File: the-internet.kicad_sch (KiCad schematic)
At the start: 9 parts, among them J1 POWER, J2 LOLIN-C3-MINI (L), J3 LOLIN-C3-MINI (R), Q1 KSC1815YTA

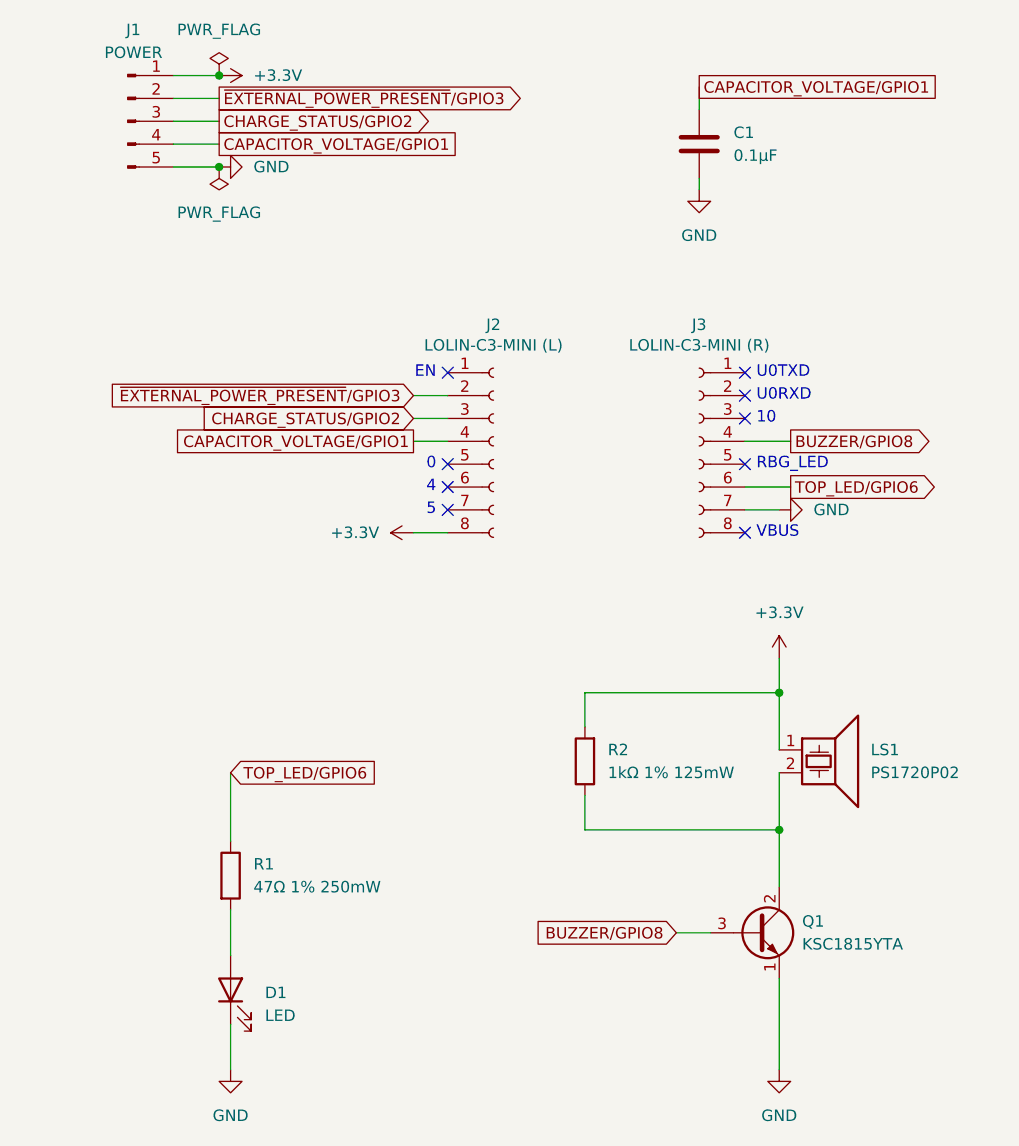
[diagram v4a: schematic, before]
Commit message: Add resistor to buzzer transistor
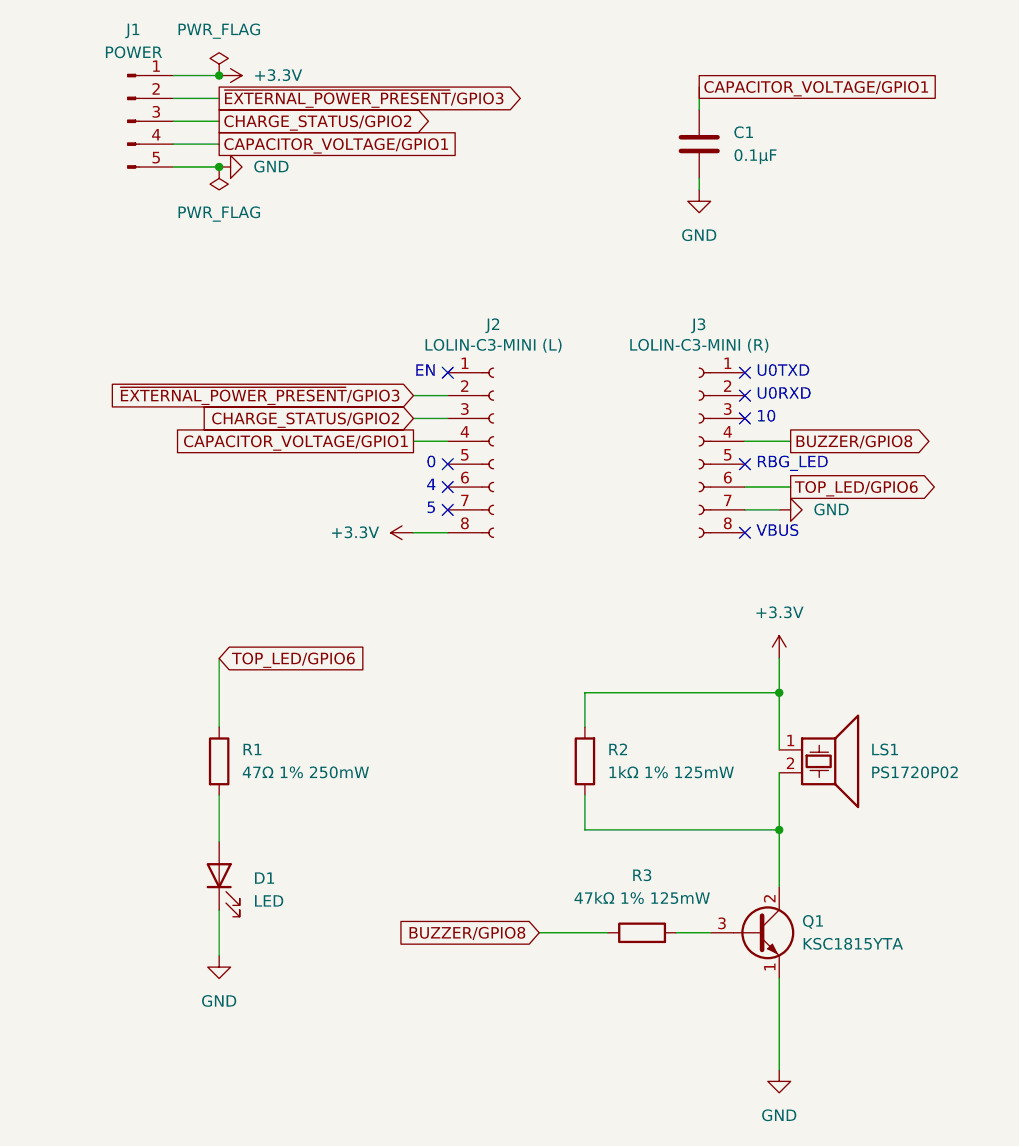
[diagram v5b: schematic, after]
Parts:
- added R3: 47kΩ 1% 125mW, Resistor_SMD:R_0805_2012Metric_Pad1.20x1.40mm_HandSolder, symbol Device:R
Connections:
- net BUZZER/GPIO8: now also R3.1; no longer Q1.3 (B)
- new net: Q1.3 (B), R3.2
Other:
- moved on the sheet: D1, R1
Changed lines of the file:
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@@
 	(wire
 		(pts
-			(xy 20.32 91.44) (xy 20.32 99.06)
+			(xy 19.05 78.74) (xy 19.05 86.36)
+		)
+		(stroke
+			(width 0)
+			(type default)
+		)
+	)
+	(wire
+		(pts
+			(xy 54.61 109.22) (xy 62.23 109.22)
 		)
 		(stroke
@@
 	(wire
 		(pts
-			(xy 20.32 106.68) (xy 20.32 111.76)
+			(xy 19.05 93.98) (xy 19.05 99.06)
 		)
 		(stroke
@@
 	(wire
 		(pts
-			(xy 20.32 119.38) (xy 20.32 124.46)
+			(xy 19.05 106.68) (xy 19.05 111.76)
 		)
 		(stroke
@@
 	(global_label "TOP_LED{slash}GPIO6"
 		(shape input)
-		(at 20.32 91.44 0)
+		(at 19.05 78.74 0)
 		(fields_autoplaced yes)
 		(effects
@@
 		)
 		(property "Intersheetrefs" "${INTERSHEET_REFS}"
-			(at 38.3033 91.44 0)
+			(at 37.0333 78.74 0)
 			(effects
 				(font
@@
 	(global_label "BUZZER{slash}GPIO8"
 		(shape input)
-		(at 69.85 109.22 180)
+		(at 54.61 109.22 180)
 		(fields_autoplaced yes)
 		(effects
@@
 		)
 		(property "Intersheetrefs" "${INTERSHEET_REFS}"
-			(at 52.411 109.22 0)
+			(at 37.171 109.22 0)
 			(effects
 				(font
@@
 	(symbol
 		(lib_id "power:GND")
-		(at 20.32 124.46 0)
+		(at 19.05 111.76 0)
 		(unit 1)
 		(exclude_from_sim no)
@@
 		(fields_autoplaced yes)
 		(property "Reference" "#PWR05"
-			(at 20.32 130.81 0)
+			(at 19.05 118.11 0)
 			(effects
 				(font
@@
 		)
 		(property "Value" "GND"
-			(at 20.32 129.54 0)
+			(at 19.05 116.84 0)
 			(effects
 				(font
@@
 		)
 		(property "Footprint" ""
-			(at 20.32 124.46 0)
+			(at 19.05 111.76 0)
 			(effects
 				(font
@@
 		)
 		(property "Datasheet" ""
-			(at 20.32 124.46 0)
+			(at 19.05 111.76 0)
 			(effects
 				(font
@@
 		)
 		(property "Description" "Power symbol creates a global label with name \"GND\" , ground"
-			(at 20.32 124.46 0)
+			(at 19.05 111.76 0)
 			(effects
 				(font
@@
 	(symbol
 		(lib_id "Device:R")
-		(at 20.32 102.87 0)
+		(at 66.04 109.22 90)
 		(unit 1)
 		(exclude_from_sim no)
@@
 		(dnp no)
 		(fields_autoplaced yes)
+		(property "Reference" "R3"
+			(at 66.04 102.87 90)
+			(effects
+				(font
+					(size 1.27 1.27)
+				)
+			)
+		)
+		(property "Value" "47kΩ 1% 125mW"
+			(at 66.04 105.41 90)
+			(effects
+				(font
+					(size 1.27 1.27)
+				)
+			)
+		)
+		(property "Footprint" "Resistor_SMD:R_0805_2012Metric_Pad1.20x1.40mm_HandSolder"
+			(at 66.04 110.998 90)
+			(effects
+				(font
+					(size 1.27 1.27)
+				)
+				(hide yes)
+			)
+		)
+		(property "Datasheet" "~"
+			(at 66.04 109.22 0)
+			(effects
+				(font
+					(size 1.27 1.27)
+				)
+				(hide yes)
+			)
+		)
+		(property "Description" "Resistor"
+			(at 66.04 109.22 0)
+			(effects
+				(font
+					(size 1.27 1.27)
+				)
+				(hide yes)
+			)
+		)
+		(pin "2"
+		)
+		(pin "1"
+		)
+		(instances
+			(project ""
+				(path "/29e3ebed-102d-4108-99f2-937621ab4bc8"
+					(reference "R3")
+					(unit 1)
+				)
+			)
+		)
+	)
+	(symbol
+		(lib_id "Device:R")
+		(at 19.05 90.17 0)
+		(unit 1)
+		(exclude_from_sim no)
+		(in_bom yes)
+		(on_board yes)
+		(dnp no)
+		(fields_autoplaced yes)
 		(property "Reference" "R1"
-			(at 22.86 101.5999 0)
+			(at 21.59 88.8999 0)
 			(effects
 				(font
@@
 		)
 		(property "Value" "47Ω 1% 250mW"
-			(at 22.86 104.1399 0)
+			(at 21.59 91.4399 0)
 			(effects
 				(font
@@
 		)
 		(property "Footprint" "Resistor_SMD:R_1206_3216Metric_Pad1.30x1.75mm_HandSolder"
-			(at 18.542 102.87 90)
+			(at 17.272 90.17 90)
 			(effects
 				(font
@@
 		)
 		(property "Datasheet" "~"
-			(at 20.32 102.87 0)
+			(at 19.05 90.17 0)
 			(effects
 				(font
@@
 		)
 		(property "Description" "Resistor"
-			(at 20.32 102.87 0)
+			(at 19.05 90.17 0)
 			(effects
 				(font
@@
 	(symbol
 		(lib_id "Device:LED")
-		(at 20.32 115.57 90)
+		(at 19.05 102.87 90)
 		(unit 1)
 		(exclude_from_sim no)
@@
 		(fields_autoplaced yes)
 		(property "Reference" "D1"
-			(at 24.13 115.8874 90)
+			(at 22.86 103.1874 90)
 			(effects
 				(font
@@
 		)
 		(property "Value" "LED"
-			(at 24.13 118.4274 90)
+			(at 22.86 105.7274 90)
 			(effects
 				(font
@@
 		)
 		(property "Footprint" "Connector_PinHeader_2.54mm:PinHeader_1x02_P2.54mm_Vertical"
-			(at 20.32 115.57 0)
+			(at 19.05 102.87 0)
 			(effects
 				(font
@@
 		)
 		(property "Datasheet" "~"
-			(at 20.32 115.57 0)
+			(at 19.05 102.87 0)
 			(effects
 				(font
@@
 		)
 		(property "Description" "Light emitting diode"
-			(at 20.32 115.57 0)
+			(at 19.05 102.87 0)
 			(effects
 				(font
@@
 		)
 		(property "Sim.Pins" "1=K 2=A"
-			(at 20.32 115.57 0)
-			(effects
-				(font
+			(at 19.05 102.87 0)
+			(effects
+				(font
